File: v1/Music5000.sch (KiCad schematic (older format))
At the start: 43 parts, among them J1 Conn_02x17_Odd_Even, J2 Conn_02x20_Odd_Even, J3 Conn_02x20_Odd_Even, J4 Conn_02x06_Top_Bottom, J5 Conn_02x06_Top_Bottom, J6 Conn_Coaxial, J7 Conn_Coaxial, J8 Conn_01x02_Male, J9 Conn_01x02_Male, Q1 2N3904, Q2 2N3904, U1 74LVC245, U2 74LVC245, U3 74LVC245, U4 IDT 71V424S12, U5 MCP4822

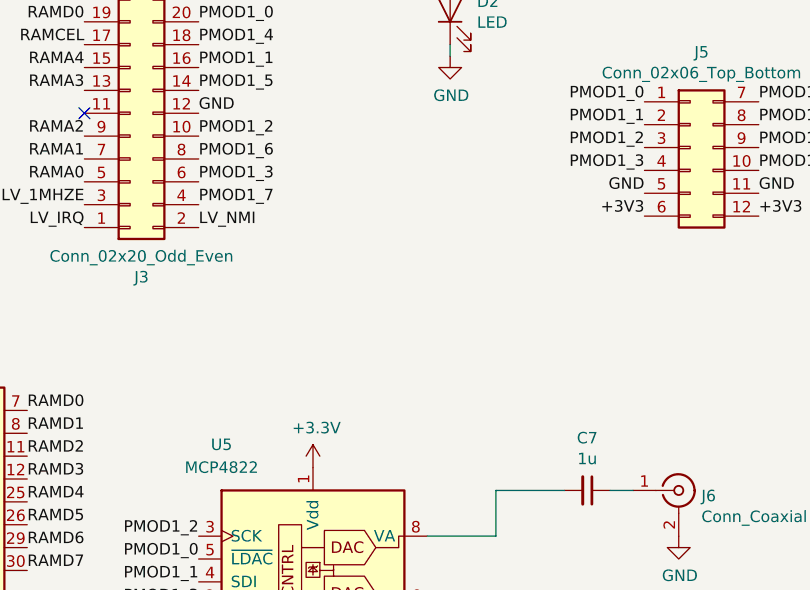
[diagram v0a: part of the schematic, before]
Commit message: PCB: Added switches
Change-Id: Ie777e91cbb6d2375a4c9e8c8aa66e1649f477c66
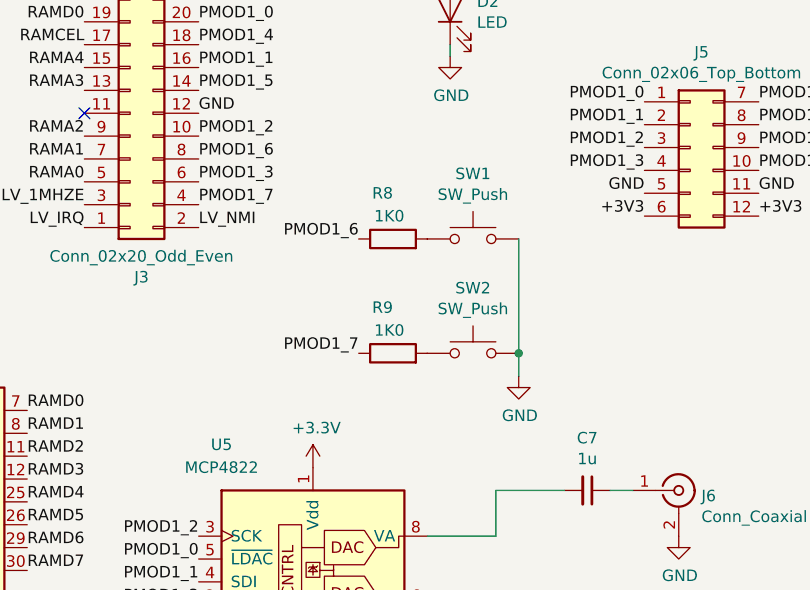
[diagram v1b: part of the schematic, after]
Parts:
- added R8, R9: 1K0, Resistor_THT:R_Axial_DIN0207_L6.3mm_D2.5mm_P10.16mm_Horizontal, symbol Device:R
- added SW1, SW2: SW_Push, Button_Switch_THT:SW_PUSH_6mm_H5mm, symbol Switch:SW_Push
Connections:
- net GND: now also SW1.2, SW2.2
- net PMOD1_6: now also R8.1
- net PMOD1_7: now also R9.1
- new net: R8.2, SW1.1
- new net: R9.2, SW2.1
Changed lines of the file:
@@
 Wire Wire Line
 	1550 6450 1550 6600
+$Comp
+L Switch:SW_Push SW1
+U 1 1 5C7C4C64
+P 9250 3100
+F 0 "SW1" H 9250 3385 50  0000 C CNN
+F 1 "SW_Push" H 9250 3294 50  0000 C CNN
+F 2 "Button_Switch_THT:SW_PUSH_6mm_H5mm" H 9250 3300 50  0001 C CNN
+F 3 "" H 9250 3300 50  0001 C CNN
+	1    9250 3100
+	1    0    0    -1
+$EndComp
+$Comp
+L Switch:SW_Push SW2
+U 1 1 5C7C4D3E
+P 9250 3600
+F 0 "SW2" H 9250 3885 50  0000 C CNN
+F 1 "SW_Push" H 9250 3794 50  0000 C CNN
+F 2 "Button_Switch_THT:SW_PUSH_6mm_H5mm" H 9250 3800 50  0001 C CNN
+F 3 "" H 9250 3800 50  0001 C CNN
+	1    9250 3600
+	1    0    0    -1
+$EndComp
+Text Label 8750 3100 2    50   ~ 0
+PMOD1_6
+Text Label 8750 3600 2    50   ~ 0
+PMOD1_7
+Wire Wire Line
+	9450 3100 9450 3600
+$Comp
+L power:GND #PWR021
+U 1 1 5C7C7AF9
+P 9450 3700
+F 0 "#PWR021" H 9450 3450 50  0001 C CNN
+F 1 "GND" H 9455 3527 50  0000 C CNN
+F 2 "" H 9450 3700 50  0001 C CNN
+F 3 "" H 9450 3700 50  0001 C CNN
+	1    9450 3700
+	1    0    0    -1
+$EndComp
+Wire Wire Line
+	9450 3600 9450 3700
+Connection ~ 9450 3600
+$Comp
+L Device:R R8
+U 1 1 5C7D1F77
+P 8900 3100
+F 0 "R8" V 9100 3100 50  0000 L CNN
+F 1 "1K0" V 9000 3050 50  0000 L CNN
+F 2 "Resistor_THT:R_Axial_DIN0207_L6.3mm_D2.5mm_P10.16mm_Horizontal" V 8830 3100 50  0001 C CNN
+F 3 "~" H 8900 3100 50  0001 C CNN
+	1    8900 3100
+	0    -1   -1   0
+$EndComp
+$Comp
+L Device:R R9
+U 1 1 5C7D51EB
+P 8900 3600
+F 0 "R9" V 9100 3600 50  0000 L CNN
+F 1 "1K0" V 9000 3550 50  0000 L CNN
+F 2 "Resistor_THT:R_Axial_DIN0207_L6.3mm_D2.5mm_P10.16mm_Horizontal" V 8830 3600 50  0001 C CNN
+F 3 "~" H 8900 3600 50  0001 C CNN
+	1    8900 3600
+	0    -1   -1   0
+$EndComp
 $EndSCHEMATC
